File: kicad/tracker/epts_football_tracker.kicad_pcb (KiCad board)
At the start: 4 copper layers, 42 x 72 mm, 46 parts, among them J1 USB4105-GF-A, J2 Li-Po 1S, J3 DM3AT-SF-PEJM5, J4 TC2030-IDC-NL, Q1 AO3401A, SW1 TL3342, U1 NEO-M9N-00B, U2 MDBT50Q-1MV2, U3 ISM330DHCX, U4 MCP73831-2-OT, U5 AP2112K-3.3, U6 USBLC6-2SC6

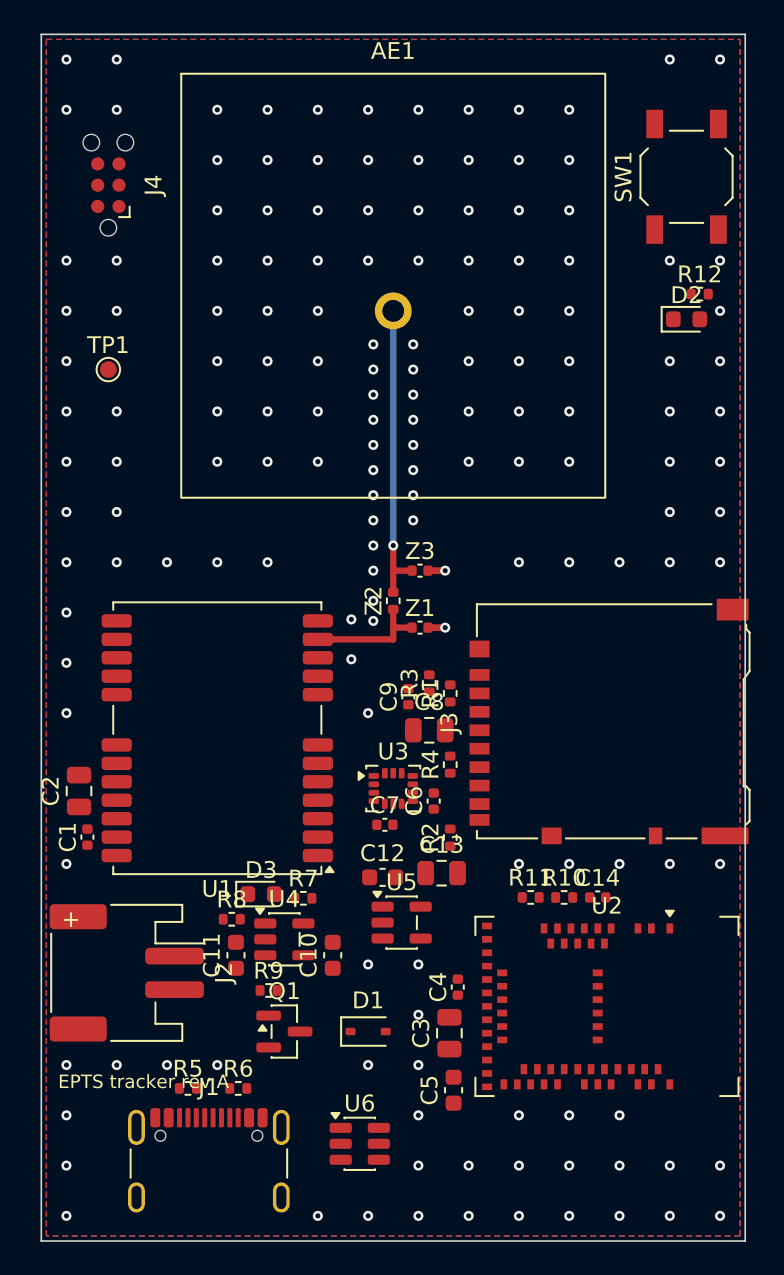
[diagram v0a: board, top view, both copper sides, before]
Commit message: Tracker: GND fan-out and all power nets routed by the generator
tracker_router.py: a GND via beside every top-layer ground pad, joined by a
short track, and an A* maze router (0.1 mm grid, F.Cu/B.Cu plus vias,
clearance-inflated obstacles, keep-outs honoured) that routes VBUS, VBAT,
VSYS and +3V3 to every pad, then string-pulls each path into 45-degree runs.
U1's RF-side ground pads go straight to the RF via fence.

check_tracker.py now checks every track and via against every other net's
copper, holes, board edge and keep-outs, checks that each power net is one
piece by KiCad's anchor rule, and checks that every GND pad has its own via.
Deleting a power track or moving a via onto another net fails it. The older
via checks use exact rectangle geometry instead of circles.

Left for KiCad: 34 signal nets, about 45 connections.

Co-Authored-By: Claude Opus 5.5 <noreply@anthropic.com>
Claude-Session: https://claude.ai/code/session_011RNuSdJ5XMwLG7Tv2CwEFd
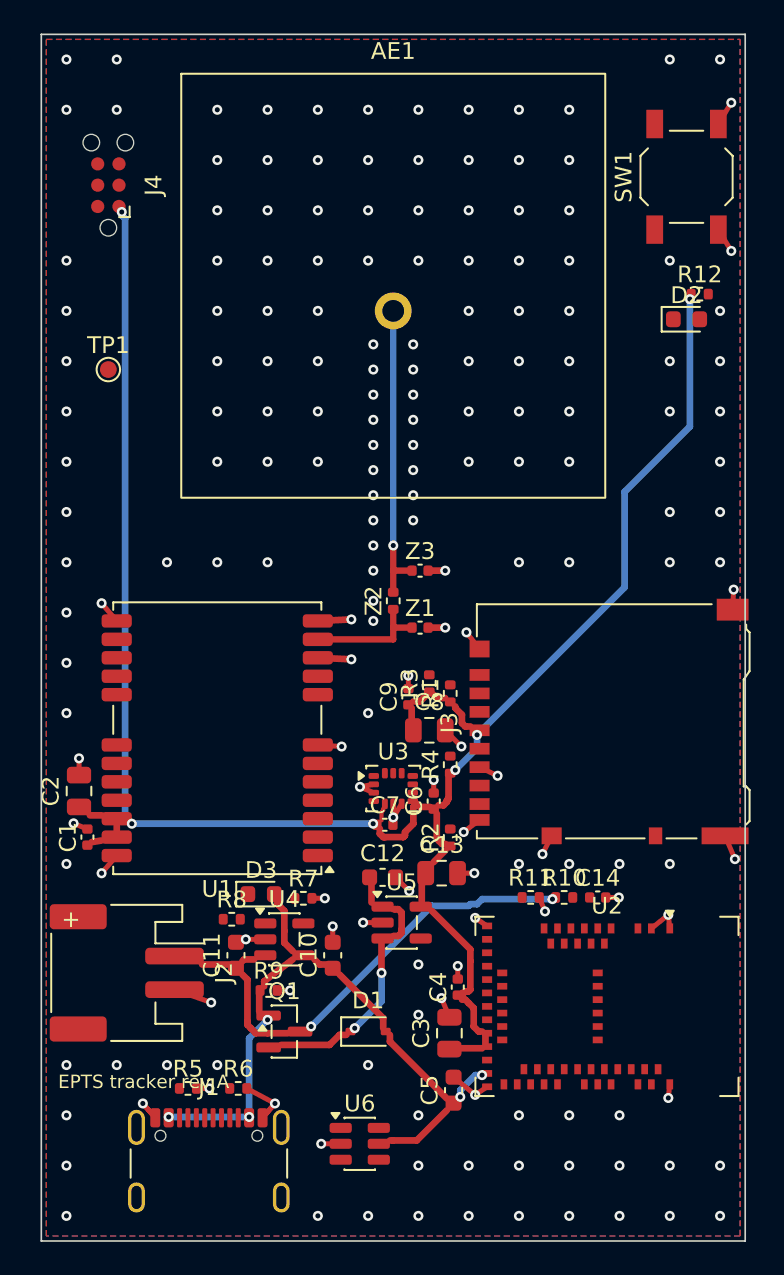
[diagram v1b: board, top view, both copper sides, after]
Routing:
- net +3V3: track 0.00 -> 113.3 mm, vias 0 -> 6
- net GND: track 2.04 -> 57.8 mm, vias 160 -> 186
- net VBUS: track 0.00 -> 34.4 mm, vias 0 -> 5
- net VBAT: track 0.00 -> 25.6 mm, vias 0 -> 2
- net VSYS: track 0.00 -> 13.4 mm, vias 0 -> 2
